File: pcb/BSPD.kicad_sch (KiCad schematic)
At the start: 59 parts, among them J1 Test header, J2 Conn_02x06_Counter_Clockwise, Q1 AO3400A, U1 LM339, U2 LM339, U3 74HC32, U4 74HC02

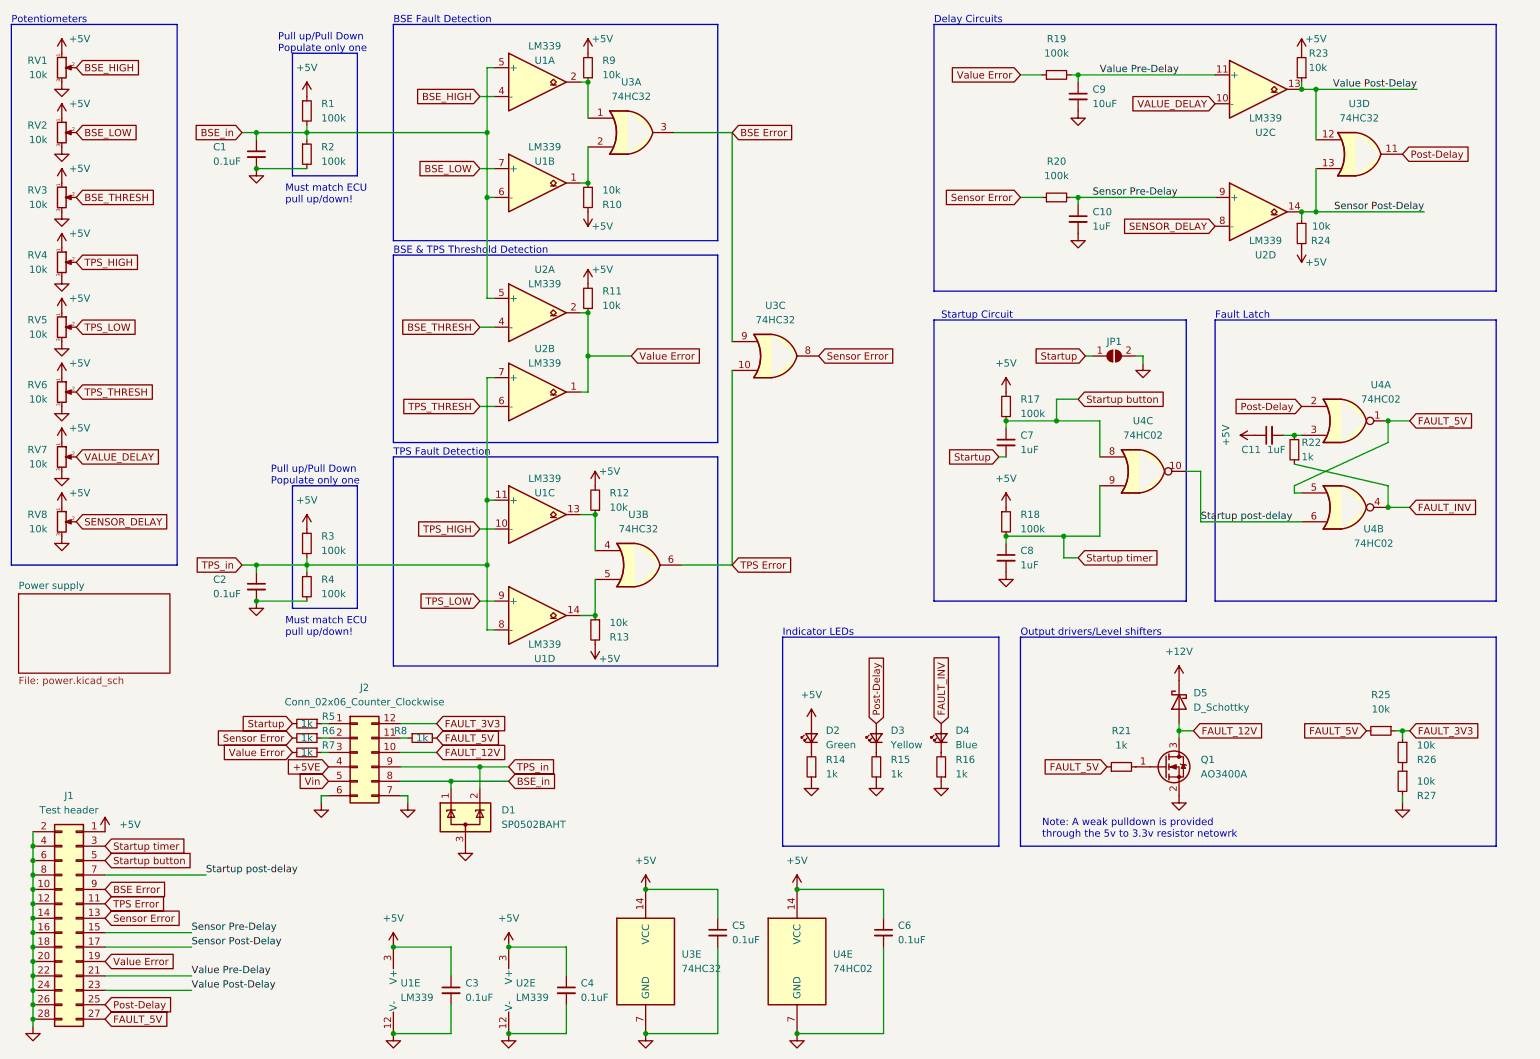
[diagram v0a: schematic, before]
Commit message: Switch to M12 Connector, fix comparator issue from rev 5
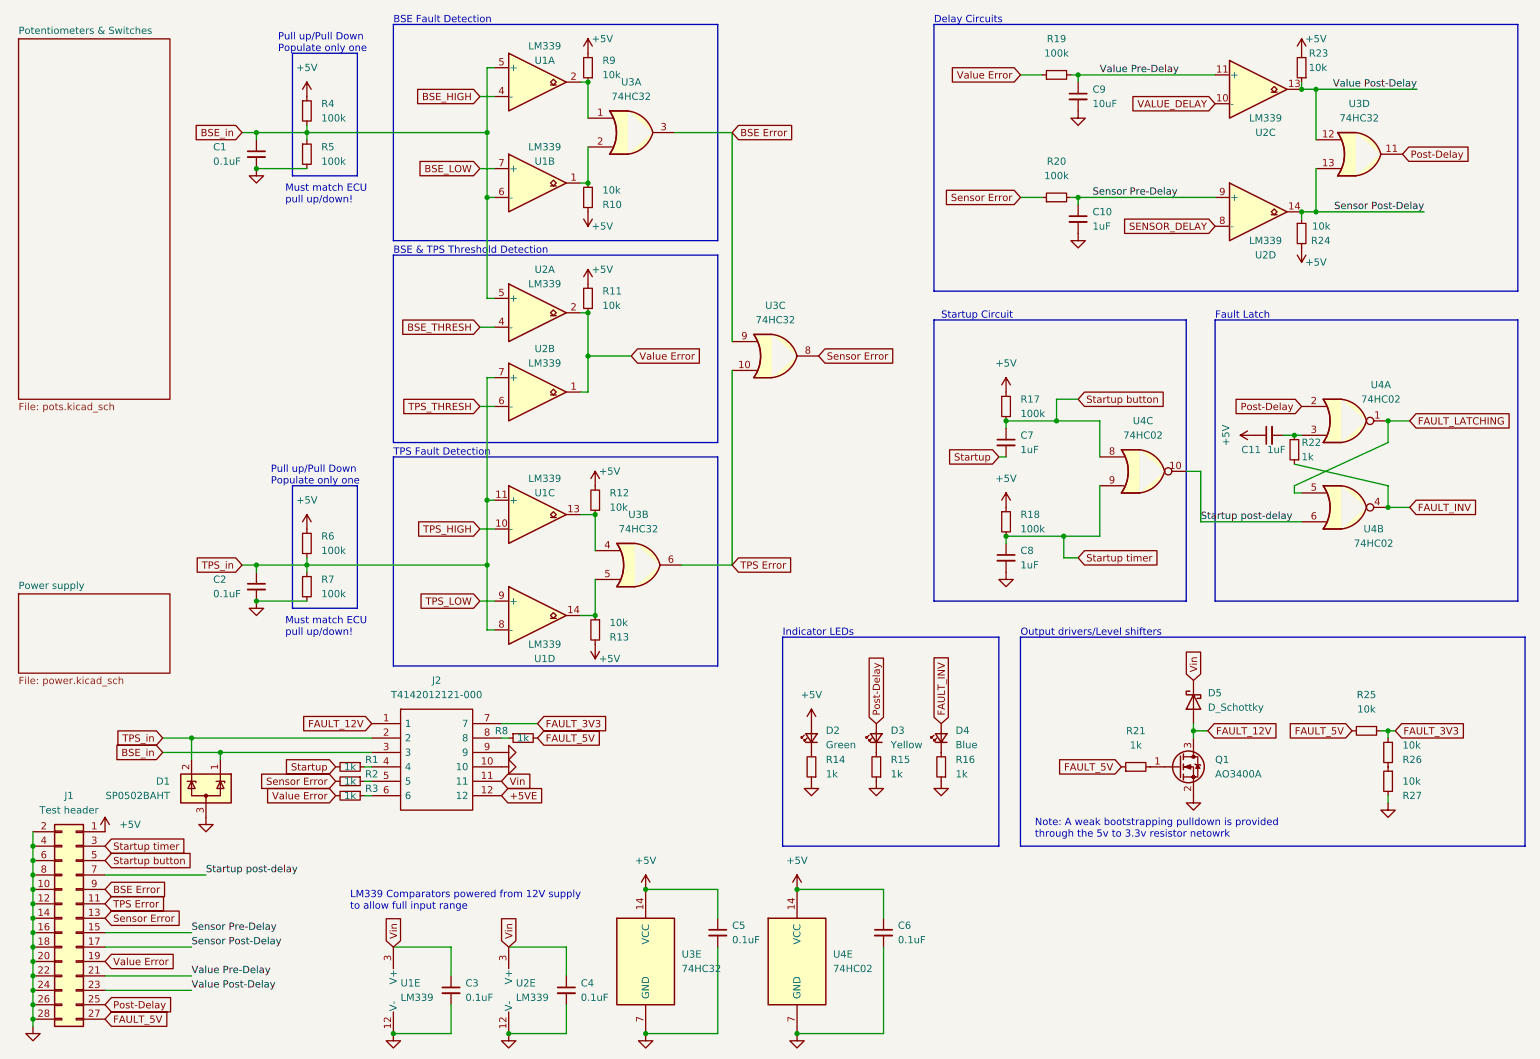
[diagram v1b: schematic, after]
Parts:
- removed J2: Conn_02x06_Counter_Clockwise, libraries:TE_DT15-12PA, symbol Connector_Generic:Conn_02x06_Counter_Clockwise
- removed JP1: SolderJumper_2_Open, Jumper:SolderJumper-2_P1.3mm_Open_RoundedPad1.0x1.5mm, symbol Jumper:SolderJumper_2_Open
- removed RV1, RV2, RV3, RV4, RV5, RV6, RV7, RV8: 10k, Potentiometer_SMD:Potentiometer_Bourns_TC33X_Vertical, symbol Device:R_Potentiometer_Small
- added J2: T4142012121-000, M12_TE_T4142012121-000:T4140012121000, symbol T4142012121-000:T4142012121-000
- renumbered R5 to R1, R6 to R2, R7 to R3, R1 to R4, R2 to R5, R3 to R6, R4 to R7
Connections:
- net +12V is gone; now on net Vin: D5.1 (K)
- net +5V: no longer C3.1, C4.1, U1.3 (V+), U2.3 (V+)
- net +5VE: now also J2.12
- net BSE_in: now also J2.3
- net FAULT_12V: now also J2.1
- net FAULT_3V3: now also J2.7
- net FAULT_5V: no longer U4.1, U4.5
- net GND: now also J2.10, J2.9
- net TPS_in: now also J2.2
- net Vin: now also C3.1, C4.1, U1.3 (V+), U2.3 (V+), J2.11
- net at R2.1: now also J2.5
- net at R1.1: now also J2.4
- net at R8.1: now also J2.8
- net at R3.1: now also J2.6
- new net FAULT_LATCHING: U4.1, U4.5
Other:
- added sheet Potentiometers & Switches (pots.kicad_sch)
- note added: "LM339 Comparators powered from 12V supply to allow full input range"
- note added: "Note: A weak bootstrapping pulldown is provided through the 5v to 3.3v resistor netowrk"
- note removed: "Note: A weak pulldown is provided through the 5v to 3.3v resistor netowrk"
- note removed: "Potentiometers"
- moved on the sheet: D1, D5, Q1, R1, R2, R21, R25, R26, R27, R3, R8

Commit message: Update to KiCad 7, bump project revision/date
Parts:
- C1, C2, C3, C4, C5, C6: Spice_Model 0.1u -> (none); Spice_Netlist_Enabled Y -> (none); Spice_Primitive C -> (none)
- C10, C11, C7, C8: Spice_Model 1u -> (none); Spice_Netlist_Enabled Y -> (none); Spice_Primitive C -> (none)
- C9: Spice_Model 10u -> (none); Spice_Netlist_Enabled Y -> (none); Spice_Primitive C -> (none)
- D1: Spice_Model SP0502BAHT -> (none); Spice_Netlist_Enabled N -> (none); Spice_Primitive D -> (none)
- D5: Spice_Model D_Schottky -> (none); Spice_Netlist_Enabled N -> (none); Spice_Primitive D -> (none)
- R10, R11, R12, R13, R23, R24, R25, R26, R27, R9: Spice_Model 10k -> (none); Spice_Netlist_Enabled Y -> (none); Spice_Primitive R -> (none)
- R17, R18, R19, R20, R4, R6: Spice_Model 100k -> (none); Spice_Netlist_Enabled Y -> (none); Spice_Primitive R -> (none)
- R5, R7: Spice_Model 100k -> (none); Spice_Netlist_Enabled N -> (none); Spice_Primitive R -> (none)
- U1, U2: Spice_Lib_File SPICE models/lmx39_spice.lib -> (none); Spice_Model LM339 -> (none); Spice_Netlist_Enabled Y -> (none); Spice_Primitive X -> (none)
- U3: Spice_Lib_File SPICE models/74hc32.lib -> (none); Spice_Model 74HC32_pkg -> (none); Spice_Netlist_Enabled Y -> (none); Spice_Primitive X -> (none)
- U4: Spice_Lib_File SPICE models/74hc02.lib -> (none); Spice_Model 74HC02_pkg -> (none); Spice_Netlist_Enabled Y -> (none); Spice_Primitive X -> (none)
